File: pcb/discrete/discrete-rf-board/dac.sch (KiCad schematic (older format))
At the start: 19 parts, among them Q20 Q_NPN_BCE

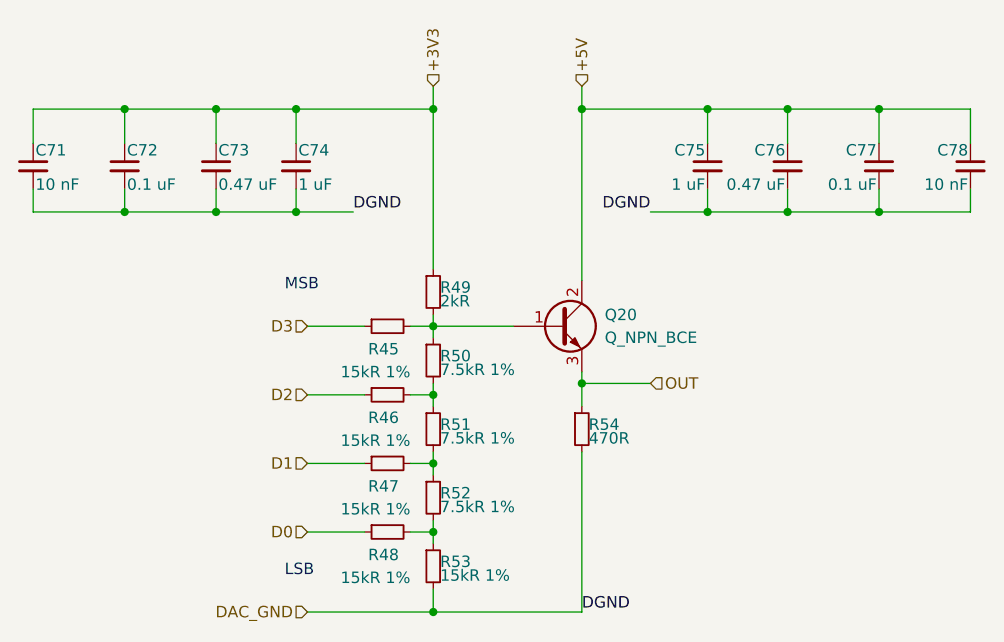
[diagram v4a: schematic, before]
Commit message: All component values set (TODO change transistor gain stages to match values from experimentation
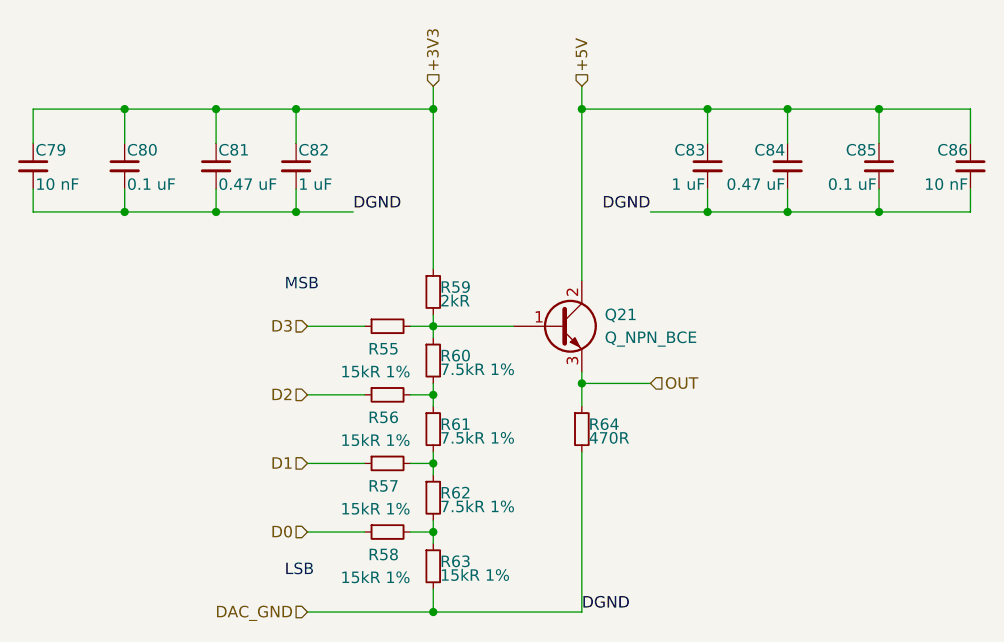
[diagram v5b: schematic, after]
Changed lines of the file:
@@
 AR Path="/5CA6B0B3/5D83265A/5D9928CB" Ref="R49"  Part="1"
 AR Path="/5CA6B0B3/5D9A8CAE/5D9928CB" Ref="R59"  Part="1"
-F 0 "R49" H 3580 2720 50  0000 L CNN
+F 0 "R59" H 3580 2720 50  0000 L CNN
 F 1 "2kR" H 3580 2660 50  0000 L CNN
 F 2 "" H 3550 2700 50  0001 C CNN
@@
 AR Path="/5CA6B0B3/5D83265A/5D992BF1" Ref="R50"  Part="1"
 AR Path="/5CA6B0B3/5D9A8CAE/5D992BF1" Ref="R60"  Part="1"
-F 0 "R50" H 3580 3020 50  0000 L CNN
+F 0 "R60" H 3580 3020 50  0000 L CNN
 F 1 "7.5kR 1%" H 3580 2960 50  0000 L CNN
 F 2 "" H 3550 3000 50  0001 C CNN
@@
 AR Path="/5CA6B0B3/5D83265A/5D9933B9" Ref="R51"  Part="1"
 AR Path="/5CA6B0B3/5D9A8CAE/5D9933B9" Ref="R61"  Part="1"
-F 0 "R51" H 3580 3320 50  0000 L CNN
+F 0 "R61" H 3580 3320 50  0000 L CNN
 F 1 "7.5kR 1%" H 3580 3260 50  0000 L CNN
 F 2 "" H 3550 3300 50  0001 C CNN
@@
 AR Path="/5CA6B0B3/5D83265A/5D993558" Ref="R52"  Part="1"
 AR Path="/5CA6B0B3/5D9A8CAE/5D993558" Ref="R62"  Part="1"
-F 0 "R52" H 3580 3620 50  0000 L CNN
+F 0 "R62" H 3580 3620 50  0000 L CNN
 F 1 "7.5kR 1%" H 3580 3560 50  0000 L CNN
 F 2 "" H 3550 3600 50  0001 C CNN
@@
 AR Path="/5CA6B0B3/5D83265A/5D993922" Ref="R53"  Part="1"
 AR Path="/5CA6B0B3/5D9A8CAE/5D993922" Ref="R63"  Part="1"
-F 0 "R53" H 3580 3920 50  0000 L CNN
+F 0 "R63" H 3580 3920 50  0000 L CNN
 F 1 "15kR 1%" H 3580 3860 50  0000 L CNN
 F 2 "" H 3550 3900 50  0001 C CNN
@@
 AR Path="/5CA6B0B3/5D83265A/5D994F7A" Ref="R45"  Part="1"
 AR Path="/5CA6B0B3/5D9A8CAE/5D994F7A" Ref="R55"  Part="1"
-F 0 "R45" V 3450 2800 50  0000 L CNN
+F 0 "R55" V 3450 2800 50  0000 L CNN
 F 1 "15kR 1%" V 3550 2750 50  0000 L CNN
 F 2 "" H 3350 2850 50  0001 C CNN
@@
 AR Path="/5CA6B0B3/5D83265A/5D996451" Ref="R46"  Part="1"
 AR Path="/5CA6B0B3/5D9A8CAE/5D996451" Ref="R56"  Part="1"
-F 0 "R46" V 3450 3100 50  0000 L CNN
+F 0 "R56" V 3450 3100 50  0000 L CNN
 F 1 "15kR 1%" V 3550 3050 50  0000 L CNN
 F 2 "" H 3350 3150 50  0001 C CNN
@@
 AR Path="/5CA6B0B3/5D83265A/5D99666E" Ref="R47"  Part="1"
 AR Path="/5CA6B0B3/5D9A8CAE/5D99666E" Ref="R57"  Part="1"
-F 0 "R47" V 3450 3400 50  0000 L CNN
+F 0 "R57" V 3450 3400 50  0000 L CNN
 F 1 "15kR 1%" V 3550 3350 50  0000 L CNN
 F 2 "" H 3350 3450 50  0001 C CNN
@@
 AR Path="/5CA6B0B3/5D83265A/5D99690F" Ref="R48"  Part="1"
 AR Path="/5CA6B0B3/5D9A8CAE/5D99690F" Ref="R58"  Part="1"
-F 0 "R48" V 3450 3700 50  0000 L CNN
+F 0 "R58" V 3450 3700 50  0000 L CNN
 F 1 "15kR 1%" V 3550 3650 50  0000 L CNN
 F 2 "" H 3350 3750 50  0001 C CNN
@@
 AR Path="/5CA6B0B3/5D83265A/5D998D16" Ref="Q20"  Part="1"
 AR Path="/5CA6B0B3/5D9A8CAE/5D998D16" Ref="Q21"  Part="1"
-F 0 "Q20" H 4300 2900 50  0000 L CNN
+F 0 "Q21" H 4300 2900 50  0000 L CNN
 F 1 "Q_NPN_BCE" H 4300 2800 50  0000 L CNN
 F 2 "" H 4300 2950 50  0001 C CNN
@@
 AR Path="/5CA6B0B3/5D83265A/5D99E2FA" Ref="R54"  Part="1"
 AR Path="/5CA6B0B3/5D9A8CAE/5D99E2FA" Ref="R64"  Part="1"
-F 0 "R54" H 4230 3320 50  0000 L CNN
+F 0 "R64" H 4230 3320 50  0000 L CNN
 F 1 "470R" H 4230 3260 50  0000 L CNN
 F 2 "" H 4200 3300 50  0001 C CNN
@@
 AR Path="/5CA6B0B3/5D83265A/5DC04556" Ref="C74"  Part="1"
 AR Path="/5CA6B0B3/5D9A8CAE/5DC04556" Ref="C82"  Part="1"
-F 0 "C74" H 2960 2220 50  0000 L CNN
+F 0 "C82" H 2960 2220 50  0000 L CNN
 F 1 "1 uF" H 2960 2070 50  0000 L CNN
 F 2 "" H 2950 2150 50  0001 C CNN
@@
 AR Path="/5CA6B0B3/5D83265A/5DC04C84" Ref="C73"  Part="1"
 AR Path="/5CA6B0B3/5D9A8CAE/5DC04C84" Ref="C81"  Part="1"
-F 0 "C73" H 2610 2220 50  0000 L CNN
+F 0 "C81" H 2610 2220 50  0000 L CNN
 F 1 "0.47 uF" H 2610 2070 50  0000 L CNN
 F 2 "" H 2600 2150 50  0001 C CNN
@@
 AR Path="/5CA6B0B3/5D83265A/5DC04F33" Ref="C72"  Part="1"
 AR Path="/5CA6B0B3/5D9A8CAE/5DC04F33" Ref="C80"  Part="1"
-F 0 "C72" H 2210 2220 50  0000 L CNN
+F 0 "C80" H 2210 2220 50  0000 L CNN
 F 1 "0.1 uF" H 2210 2070 50  0000 L CNN
 F 2 "" H 2200 2150 50  0001 C CNN
@@
 AR Path="/5CA6B0B3/5D83265A/5DC05279" Ref="C71"  Part="1"
 AR Path="/5CA6B0B3/5D9A8CAE/5DC05279" Ref="C79"  Part="1"
-F 0 "C71" H 1810 2220 50  0000 L CNN
+F 0 "C79" H 1810 2220 50  0000 L CNN
 F 1 "10 nF" H 1810 2070 50  0000 L CNN
 F 2 "" H 1800 2150 50  0001 C CNN
@@
 AR Path="/5CA6B0B3/5D83265A/5DC0F871" Ref="C75"  Part="1"
 AR Path="/5CA6B0B3/5D9A8CAE/5DC0F871" Ref="C83"  Part="1"
-F 0 "C75" H 4760 2220 50  0000 L CNN
+F 0 "C83" H 4760 2220 50  0000 L CNN
 F 1 "1 uF" H 4760 2070 50  0000 L CNN
 F 2 "" H 4750 2150 50  0001 C CNN
@@
 AR Path="/5CA6B0B3/5D83265A/5DC0F877" Ref="C76"  Part="1"
 AR Path="/5CA6B0B3/5D9A8CAE/5DC0F877" Ref="C84"  Part="1"
-F 0 "C76" H 5110 2220 50  0000 L CNN
+F 0 "C84" H 5110 2220 50  0000 L CNN
 F 1 "0.47 uF" H 5110 2070 50  0000 L CNN
 F 2 "" H 5100 2150 50  0001 C CNN
@@
 AR Path="/5CA6B0B3/5D83265A/5DC0F87D" Ref="C77"  Part="1"
 AR Path="/5CA6B0B3/5D9A8CAE/5DC0F87D" Ref="C85"  Part="1"
-F 0 "C77" H 5510 2220 50  0000 L CNN
+F 0 "C85" H 5510 2220 50  0000 L CNN
 F 1 "0.1 uF" H 5510 2070 50  0000 L CNN
 F 2 "" H 5500 2150 50  0001 C CNN
@@
 AR Path="/5CA6B0B3/5D83265A/5DC0F883" Ref="C78"  Part="1"
 AR Path="/5CA6B0B3/5D9A8CAE/5DC0F883" Ref="C86"  Part="1"
-F 0 "C78" H 5910 2220 50  0000 L CNN
+F 0 "C86" H 5910 2220 50  0000 L CNN
 F 1 "10 nF" H 5910 2070 50  0000 L CNN
 F 2 "" H 5900 2150 50  0001 C CNN

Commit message: Footprint some stuff
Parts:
- C73: footprint (none) -> Capacitor_SMD:C_0402_1005Metric; Mouser (none) -> 963-JMK105BJ474MV-F
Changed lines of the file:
@@
 AR Path="/5CA6B0B3/5D83265A/5D9928CB" Ref="R49"  Part="1"
 AR Path="/5CA6B0B3/5D9A8CAE/5D9928CB" Ref="R59"  Part="1"
-F 0 "R59" H 3580 2720 50  0000 L CNN
+F 0 "R49" H 3580 2720 50  0000 L CNN
 F 1 "2kR" H 3580 2660 50  0000 L CNN
 F 2 "" H 3550 2700 50  0001 C CNN
@@
 AR Path="/5CA6B0B3/5D83265A/5D992BF1" Ref="R50"  Part="1"
 AR Path="/5CA6B0B3/5D9A8CAE/5D992BF1" Ref="R60"  Part="1"
-F 0 "R60" H 3580 3020 50  0000 L CNN
+F 0 "R50" H 3580 3020 50  0000 L CNN
 F 1 "7.5kR 1%" H 3580 2960 50  0000 L CNN
 F 2 "" H 3550 3000 50  0001 C CNN
@@
 AR Path="/5CA6B0B3/5D83265A/5D9933B9" Ref="R51"  Part="1"
 AR Path="/5CA6B0B3/5D9A8CAE/5D9933B9" Ref="R61"  Part="1"
-F 0 "R61" H 3580 3320 50  0000 L CNN
+F 0 "R51" H 3580 3320 50  0000 L CNN
 F 1 "7.5kR 1%" H 3580 3260 50  0000 L CNN
 F 2 "" H 3550 3300 50  0001 C CNN
@@
 AR Path="/5CA6B0B3/5D83265A/5D993558" Ref="R52"  Part="1"
 AR Path="/5CA6B0B3/5D9A8CAE/5D993558" Ref="R62"  Part="1"
-F 0 "R62" H 3580 3620 50  0000 L CNN
+F 0 "R52" H 3580 3620 50  0000 L CNN
 F 1 "7.5kR 1%" H 3580 3560 50  0000 L CNN
 F 2 "" H 3550 3600 50  0001 C CNN
@@
 AR Path="/5CA6B0B3/5D83265A/5D993922" Ref="R53"  Part="1"
 AR Path="/5CA6B0B3/5D9A8CAE/5D993922" Ref="R63"  Part="1"
-F 0 "R63" H 3580 3920 50  0000 L CNN
+F 0 "R53" H 3580 3920 50  0000 L CNN
 F 1 "15kR 1%" H 3580 3860 50  0000 L CNN
 F 2 "" H 3550 3900 50  0001 C CNN
@@
 AR Path="/5CA6B0B3/5D83265A/5D994F7A" Ref="R45"  Part="1"
 AR Path="/5CA6B0B3/5D9A8CAE/5D994F7A" Ref="R55"  Part="1"
-F 0 "R55" V 3450 2800 50  0000 L CNN
+F 0 "R45" V 3450 2800 50  0000 L CNN
 F 1 "15kR 1%" V 3550 2750 50  0000 L CNN
 F 2 "" H 3350 2850 50  0001 C CNN
@@
 AR Path="/5CA6B0B3/5D83265A/5D996451" Ref="R46"  Part="1"
 AR Path="/5CA6B0B3/5D9A8CAE/5D996451" Ref="R56"  Part="1"
-F 0 "R56" V 3450 3100 50  0000 L CNN
+F 0 "R46" V 3450 3100 50  0000 L CNN
 F 1 "15kR 1%" V 3550 3050 50  0000 L CNN
 F 2 "" H 3350 3150 50  0001 C CNN
@@
 AR Path="/5CA6B0B3/5D83265A/5D99666E" Ref="R47"  Part="1"
 AR Path="/5CA6B0B3/5D9A8CAE/5D99666E" Ref="R57"  Part="1"
-F 0 "R57" V 3450 3400 50  0000 L CNN
+F 0 "R47" V 3450 3400 50  0000 L CNN
 F 1 "15kR 1%" V 3550 3350 50  0000 L CNN
 F 2 "" H 3350 3450 50  0001 C CNN
@@
 AR Path="/5CA6B0B3/5D83265A/5D99690F" Ref="R48"  Part="1"
 AR Path="/5CA6B0B3/5D9A8CAE/5D99690F" Ref="R58"  Part="1"
-F 0 "R58" V 3450 3700 50  0000 L CNN
+F 0 "R48" V 3450 3700 50  0000 L CNN
 F 1 "15kR 1%" V 3550 3650 50  0000 L CNN
 F 2 "" H 3350 3750 50  0001 C CNN
@@
 AR Path="/5CA6B0B3/5D83265A/5D998D16" Ref="Q20"  Part="1"
 AR Path="/5CA6B0B3/5D9A8CAE/5D998D16" Ref="Q21"  Part="1"
-F 0 "Q21" H 4300 2900 50  0000 L CNN
+F 0 "Q20" H 4300 2900 50  0000 L CNN
 F 1 "Q_NPN_BCE" H 4300 2800 50  0000 L CNN
 F 2 "" H 4300 2950 50  0001 C CNN
@@
 AR Path="/5CA6B0B3/5D83265A/5D99E2FA" Ref="R54"  Part="1"
 AR Path="/5CA6B0B3/5D9A8CAE/5D99E2FA" Ref="R64"  Part="1"
-F 0 "R64" H 4230 3320 50  0000 L CNN
+F 0 "R54" H 4230 3320 50  0000 L CNN
 F 1 "470R" H 4230 3260 50  0000 L CNN
 F 2 "" H 4200 3300 50  0001 C CNN
@@
 AR Path="/5CA6B0B3/5D83265A/5DC04556" Ref="C74"  Part="1"
 AR Path="/5CA6B0B3/5D9A8CAE/5DC04556" Ref="C82"  Part="1"
-F 0 "C82" H 2960 2220 50  0000 L CNN
+F 0 "C74" H 2960 2220 50  0000 L CNN
 F 1 "1 uF" H 2960 2070 50  0000 L CNN
 F 2 "" H 2950 2150 50  0001 C CNN
@@
 AR Path="/5CA6B0B3/5D83265A/5DC04C84" Ref="C73"  Part="1"
 AR Path="/5CA6B0B3/5D9A8CAE/5DC04C84" Ref="C81"  Part="1"
-F 0 "C81" H 2610 2220 50  0000 L CNN
+F 0 "C73" H 2610 2220 50  0000 L CNN
 F 1 "0.47 uF" H 2610 2070 50  0000 L CNN
-F 2 "" H 2600 2150 50  0001 C CNN
+F 2 "Capacitor_SMD:C_0402_1005Metric" H 2600 2150 50  0001 C CNN
 F 3 "~" H 2600 2150 50  0001 C CNN
+F 4 "963-JMK105BJ474MV-F" H 2600 2150 50  0001 C CNN "Mouser"
 	1    2600 2150
 	1    0    0    -1
@@
 AR Path="/5CA6B0B3/5D83265A/5DC04F33" Ref="C72"  Part="1"
 AR Path="/5CA6B0B3/5D9A8CAE/5DC04F33" Ref="C80"  Part="1"
-F 0 "C80" H 2210 2220 50  0000 L CNN
+F 0 "C72" H 2210 2220 50  0000 L CNN
 F 1 "0.1 uF" H 2210 2070 50  0000 L CNN
 F 2 "" H 2200 2150 50  0001 C CNN
@@
 AR Path="/5CA6B0B3/5D83265A/5DC05279" Ref="C71"  Part="1"
 AR Path="/5CA6B0B3/5D9A8CAE/5DC05279" Ref="C79"  Part="1"
-F 0 "C79" H 1810 2220 50  0000 L CNN
+F 0 "C71" H 1810 2220 50  0000 L CNN
 F 1 "10 nF" H 1810 2070 50  0000 L CNN
 F 2 "" H 1800 2150 50  0001 C CNN
@@
 AR Path="/5CA6B0B3/5D83265A/5DC0F871" Ref="C75"  Part="1"
 AR Path="/5CA6B0B3/5D9A8CAE/5DC0F871" Ref="C83"  Part="1"
-F 0 "C83" H 4760 2220 50  0000 L CNN
+F 0 "C75" H 4760 2220 50  0000 L CNN
 F 1 "1 uF" H 4760 2070 50  0000 L CNN
 F 2 "" H 4750 2150 50  0001 C CNN
@@
 AR Path="/5CA6B0B3/5D83265A/5DC0F877" Ref="C76"  Part="1"
 AR Path="/5CA6B0B3/5D9A8CAE/5DC0F877" Ref="C84"  Part="1"
-F 0 "C84" H 5110 2220 50  0000 L CNN
+F 0 "C76" H 5110 2220 50  0000 L CNN
 F 1 "0.47 uF" H 5110 2070 50  0000 L CNN
 F 2 "" H 5100 2150 50  0001 C CNN
@@
 AR Path="/5CA6B0B3/5D83265A/5DC0F87D" Ref="C77"  Part="1"
 AR Path="/5CA6B0B3/5D9A8CAE/5DC0F87D" Ref="C85"  Part="1"
-F 0 "C85" H 5510 2220 50  0000 L CNN
+F 0 "C77" H 5510 2220 50  0000 L CNN
 F 1 "0.1 uF" H 5510 2070 50  0000 L CNN
 F 2 "" H 5500 2150 50  0001 C CNN
@@
 AR Path="/5CA6B0B3/5D83265A/5DC0F883" Ref="C78"  Part="1"
 AR Path="/5CA6B0B3/5D9A8CAE/5DC0F883" Ref="C86"  Part="1"
-F 0 "C86" H 5910 2220 50  0000 L CNN
+F 0 "C78" H 5910 2220 50  0000 L CNN
 F 1 "10 nF" H 5910 2070 50  0000 L CNN
 F 2 "" H 5900 2150 50  0001 C CNN

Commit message: Autofill
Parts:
- C76: footprint (none) -> Capacitor_SMD:C_0402_1005Metric; Mouser (none) -> 963-JMK105BJ474MV-F
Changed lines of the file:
@@
 F 0 "C76" H 5110 2220 50  0000 L CNN
 F 1 "0.47 uF" H 5110 2070 50  0000 L CNN
-F 2 "" H 5100 2150 50  0001 C CNN
+F 2 "Capacitor_SMD:C_0402_1005Metric" H 5100 2150 50  0001 C CNN
 F 3 "~" H 5100 2150 50  0001 C CNN
+F 4 "963-JMK105BJ474MV-F" H 5100 2150 50  0001 C CNN "Mouser"
 	1    5100 2150
 	-1   0    0    -1

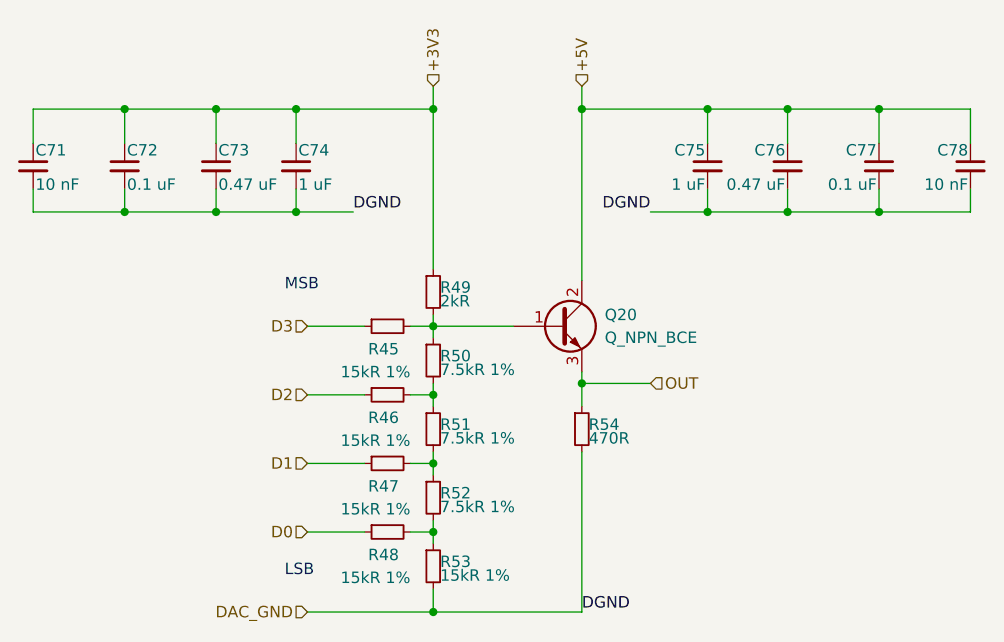
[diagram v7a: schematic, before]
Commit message: Add more footprints, saving before autofill
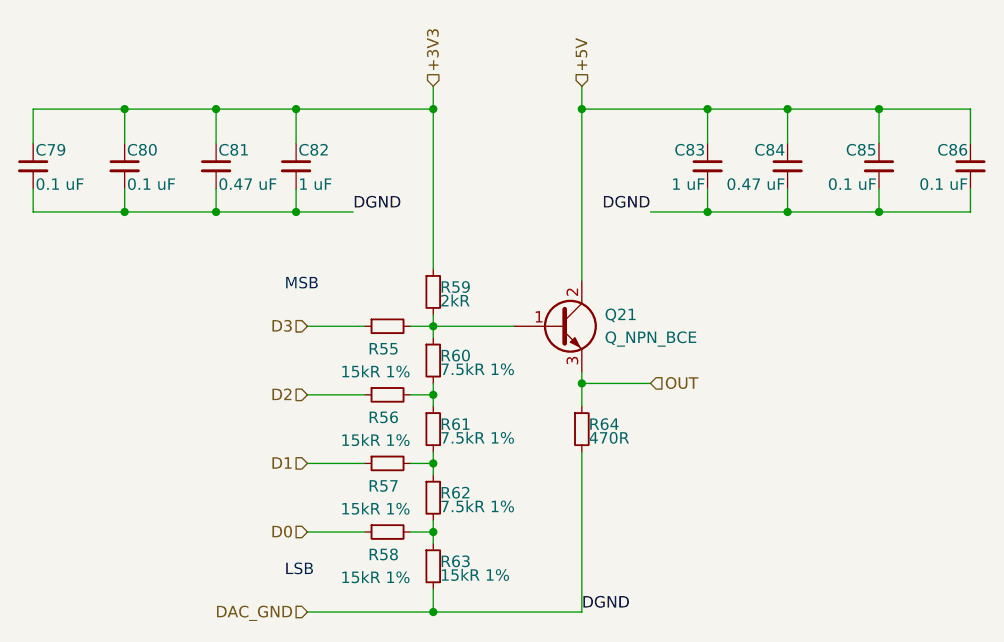
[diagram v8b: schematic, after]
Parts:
- C71, C78: value 10 nF -> 0.1 uF
- R53: footprint (none) -> Resistor_SMD:R_0805_2012Metric_Pad1.15x1.40mm_HandSolder; Mouser (none) -> 71-CRCW080515K0FKEBC
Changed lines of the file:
@@
 AR Path="/5CA6B0B3/5D83265A/5D9928CB" Ref="R49"  Part="1"
 AR Path="/5CA6B0B3/5D9A8CAE/5D9928CB" Ref="R59"  Part="1"
-F 0 "R49" H 3580 2720 50  0000 L CNN
+F 0 "R59" H 3580 2720 50  0000 L CNN
 F 1 "2kR" H 3580 2660 50  0000 L CNN
 F 2 "" H 3550 2700 50  0001 C CNN
@@
 AR Path="/5CA6B0B3/5D83265A/5D992BF1" Ref="R50"  Part="1"
 AR Path="/5CA6B0B3/5D9A8CAE/5D992BF1" Ref="R60"  Part="1"
-F 0 "R50" H 3580 3020 50  0000 L CNN
+F 0 "R60" H 3580 3020 50  0000 L CNN
 F 1 "7.5kR 1%" H 3580 2960 50  0000 L CNN
 F 2 "" H 3550 3000 50  0001 C CNN
@@
 AR Path="/5CA6B0B3/5D83265A/5D9933B9" Ref="R51"  Part="1"
 AR Path="/5CA6B0B3/5D9A8CAE/5D9933B9" Ref="R61"  Part="1"
-F 0 "R51" H 3580 3320 50  0000 L CNN
+F 0 "R61" H 3580 3320 50  0000 L CNN
 F 1 "7.5kR 1%" H 3580 3260 50  0000 L CNN
 F 2 "" H 3550 3300 50  0001 C CNN
@@
 AR Path="/5CA6B0B3/5D83265A/5D993558" Ref="R52"  Part="1"
 AR Path="/5CA6B0B3/5D9A8CAE/5D993558" Ref="R62"  Part="1"
-F 0 "R52" H 3580 3620 50  0000 L CNN
+F 0 "R62" H 3580 3620 50  0000 L CNN
 F 1 "7.5kR 1%" H 3580 3560 50  0000 L CNN
 F 2 "" H 3550 3600 50  0001 C CNN
@@
 AR Path="/5CA6B0B3/5D83265A/5D993922" Ref="R53"  Part="1"
 AR Path="/5CA6B0B3/5D9A8CAE/5D993922" Ref="R63"  Part="1"
-F 0 "R53" H 3580 3920 50  0000 L CNN
+F 0 "R63" H 3580 3920 50  0000 L CNN
 F 1 "15kR 1%" H 3580 3860 50  0000 L CNN
-F 2 "" H 3550 3900 50  0001 C CNN
+F 2 "Resistor_SMD:R_0805_2012Metric_Pad1.15x1.40mm_HandSolder" H 3550 3900 50  0001 C CNN
 F 3 "~" H 3550 3900 50  0001 C CNN
+F 4 "71-CRCW080515K0FKEBC" H 3550 3900 50  0001 C CNN "Mouser"
 	1    3550 3900
 	1    0    0    -1
@@
 AR Path="/5CA6B0B3/5D83265A/5D994F7A" Ref="R45"  Part="1"
 AR Path="/5CA6B0B3/5D9A8CAE/5D994F7A" Ref="R55"  Part="1"
-F 0 "R45" V 3450 2800 50  0000 L CNN
+F 0 "R55" V 3450 2800 50  0000 L CNN
 F 1 "15kR 1%" V 3550 2750 50  0000 L CNN
 F 2 "" H 3350 2850 50  0001 C CNN
@@
 AR Path="/5CA6B0B3/5D83265A/5D996451" Ref="R46"  Part="1"
 AR Path="/5CA6B0B3/5D9A8CAE/5D996451" Ref="R56"  Part="1"
-F 0 "R46" V 3450 3100 50  0000 L CNN
+F 0 "R56" V 3450 3100 50  0000 L CNN
 F 1 "15kR 1%" V 3550 3050 50  0000 L CNN
 F 2 "" H 3350 3150 50  0001 C CNN
@@
 AR Path="/5CA6B0B3/5D83265A/5D99666E" Ref="R47"  Part="1"
 AR Path="/5CA6B0B3/5D9A8CAE/5D99666E" Ref="R57"  Part="1"
-F 0 "R47" V 3450 3400 50  0000 L CNN
+F 0 "R57" V 3450 3400 50  0000 L CNN
 F 1 "15kR 1%" V 3550 3350 50  0000 L CNN
 F 2 "" H 3350 3450 50  0001 C CNN
@@
 AR Path="/5CA6B0B3/5D83265A/5D99690F" Ref="R48"  Part="1"
 AR Path="/5CA6B0B3/5D9A8CAE/5D99690F" Ref="R58"  Part="1"
-F 0 "R48" V 3450 3700 50  0000 L CNN
+F 0 "R58" V 3450 3700 50  0000 L CNN
 F 1 "15kR 1%" V 3550 3650 50  0000 L CNN
 F 2 "" H 3350 3750 50  0001 C CNN
@@
 AR Path="/5CA6B0B3/5D83265A/5D998D16" Ref="Q20"  Part="1"
 AR Path="/5CA6B0B3/5D9A8CAE/5D998D16" Ref="Q21"  Part="1"
-F 0 "Q20" H 4300 2900 50  0000 L CNN
+F 0 "Q21" H 4300 2900 50  0000 L CNN
 F 1 "Q_NPN_BCE" H 4300 2800 50  0000 L CNN
 F 2 "" H 4300 2950 50  0001 C CNN
@@
 AR Path="/5CA6B0B3/5D83265A/5D99E2FA" Ref="R54"  Part="1"
 AR Path="/5CA6B0B3/5D9A8CAE/5D99E2FA" Ref="R64"  Part="1"
-F 0 "R54" H 4230 3320 50  0000 L CNN
+F 0 "R64" H 4230 3320 50  0000 L CNN
 F 1 "470R" H 4230 3260 50  0000 L CNN
 F 2 "" H 4200 3300 50  0001 C CNN
@@
 AR Path="/5CA6B0B3/5D83265A/5DC04556" Ref="C74"  Part="1"
 AR Path="/5CA6B0B3/5D9A8CAE/5DC04556" Ref="C82"  Part="1"
-F 0 "C74" H 2960 2220 50  0000 L CNN
+F 0 "C82" H 2960 2220 50  0000 L CNN
 F 1 "1 uF" H 2960 2070 50  0000 L CNN
 F 2 "" H 2950 2150 50  0001 C CNN
@@
 AR Path="/5CA6B0B3/5D83265A/5DC04C84" Ref="C73"  Part="1"
 AR Path="/5CA6B0B3/5D9A8CAE/5DC04C84" Ref="C81"  Part="1"
-F 0 "C73" H 2610 2220 50  0000 L CNN
+F 0 "C81" H 2610 2220 50  0000 L CNN
 F 1 "0.47 uF" H 2610 2070 50  0000 L CNN
 F 2 "Capacitor_SMD:C_0402_1005Metric" H 2600 2150 50  0001 C CNN
@@
 AR Path="/5CA6B0B3/5D83265A/5DC04F33" Ref="C72"  Part="1"
 AR Path="/5CA6B0B3/5D9A8CAE/5DC04F33" Ref="C80"  Part="1"
-F 0 "C72" H 2210 2220 50  0000 L CNN
+F 0 "C80" H 2210 2220 50  0000 L CNN
 F 1 "0.1 uF" H 2210 2070 50  0000 L CNN
 F 2 "" H 2200 2150 50  0001 C CNN
@@
 AR Path="/5CA6B0B3/5D83265A/5DC05279" Ref="C71"  Part="1"
 AR Path="/5CA6B0B3/5D9A8CAE/5DC05279" Ref="C79"  Part="1"
-F 0 "C71" H 1810 2220 50  0000 L CNN
-F 1 "10 nF" H 1810 2070 50  0000 L CNN
+F 0 "C79" H 1810 2220 50  0000 L CNN
+F 1 "0.1 uF" H 1810 2070 50  0000 L CNN
 F 2 "" H 1800 2150 50  0001 C CNN
 F 3 "~" H 1800 2150 50  0001 C CNN
@@
 AR Path="/5CA6B0B3/5D83265A/5DC0F871" Ref="C75"  Part="1"
 AR Path="/5CA6B0B3/5D9A8CAE/5DC0F871" Ref="C83"  Part="1"
-F 0 "C75" H 4760 2220 50  0000 L CNN
+F 0 "C83" H 4760 2220 50  0000 L CNN
 F 1 "1 uF" H 4760 2070 50  0000 L CNN
 F 2 "" H 4750 2150 50  0001 C CNN
@@
 AR Path="/5CA6B0B3/5D83265A/5DC0F877" Ref="C76"  Part="1"
 AR Path="/5CA6B0B3/5D9A8CAE/5DC0F877" Ref="C84"  Part="1"
-F 0 "C76" H 5110 2220 50  0000 L CNN
+F 0 "C84" H 5110 2220 50  0000 L CNN
 F 1 "0.47 uF" H 5110 2070 50  0000 L CNN
 F 2 "Capacitor_SMD:C_0402_1005Metric" H 5100 2150 50  0001 C CNN
@@
 AR Path="/5CA6B0B3/5D83265A/5DC0F87D" Ref="C77"  Part="1"
 AR Path="/5CA6B0B3/5D9A8CAE/5DC0F87D" Ref="C85"  Part="1"
-F 0 "C77" H 5510 2220 50  0000 L CNN
+F 0 "C85" H 5510 2220 50  0000 L CNN
 F 1 "0.1 uF" H 5510 2070 50  0000 L CNN
 F 2 "" H 5500 2150 50  0001 C CNN
@@
 AR Path="/5CA6B0B3/5D83265A/5DC0F883" Ref="C78"  Part="1"
 AR Path="/5CA6B0B3/5D9A8CAE/5DC0F883" Ref="C86"  Part="1"
-F 0 "C78" H 5910 2220 50  0000 L CNN
-F 1 "10 nF" H 5910 2070 50  0000 L CNN
+F 0 "C86" H 5910 2220 50  0000 L CNN
+F 1 "0.1 uF" H 5910 2070 50  0000 L CNN
 F 2 "" H 5900 2150 50  0001 C CNN
 F 3 "~" H 5900 2150 50  0001 C CNN
